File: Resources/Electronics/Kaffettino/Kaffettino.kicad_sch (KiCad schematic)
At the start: 39 parts, among them J2 OSTVN02A150, J3 OSTVN04A150, J4 OSTVN04A150, J5 OSTVN04A150, M1 RFID-RC522, Q1 PN2222A, U1 PCF8574AN, U2 DFR0299, U3 ESP32-38Pin-Wroom, U4 26052

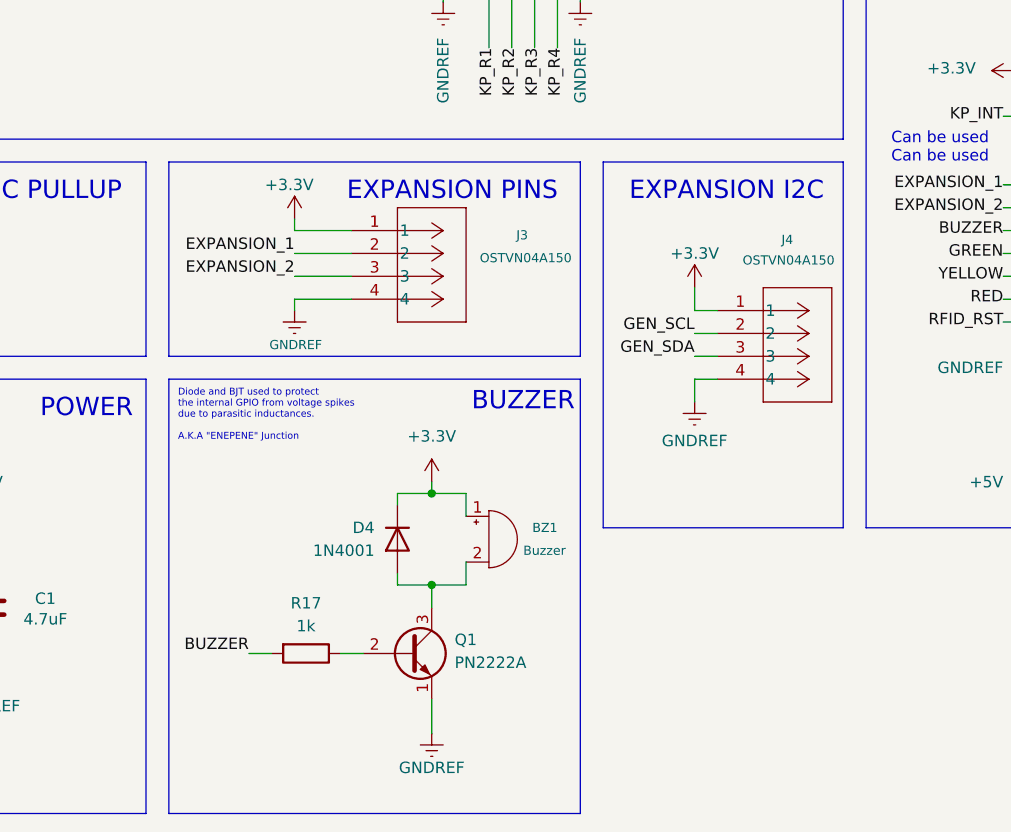
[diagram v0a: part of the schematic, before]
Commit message: Embedded: Added 5V to expansion headers
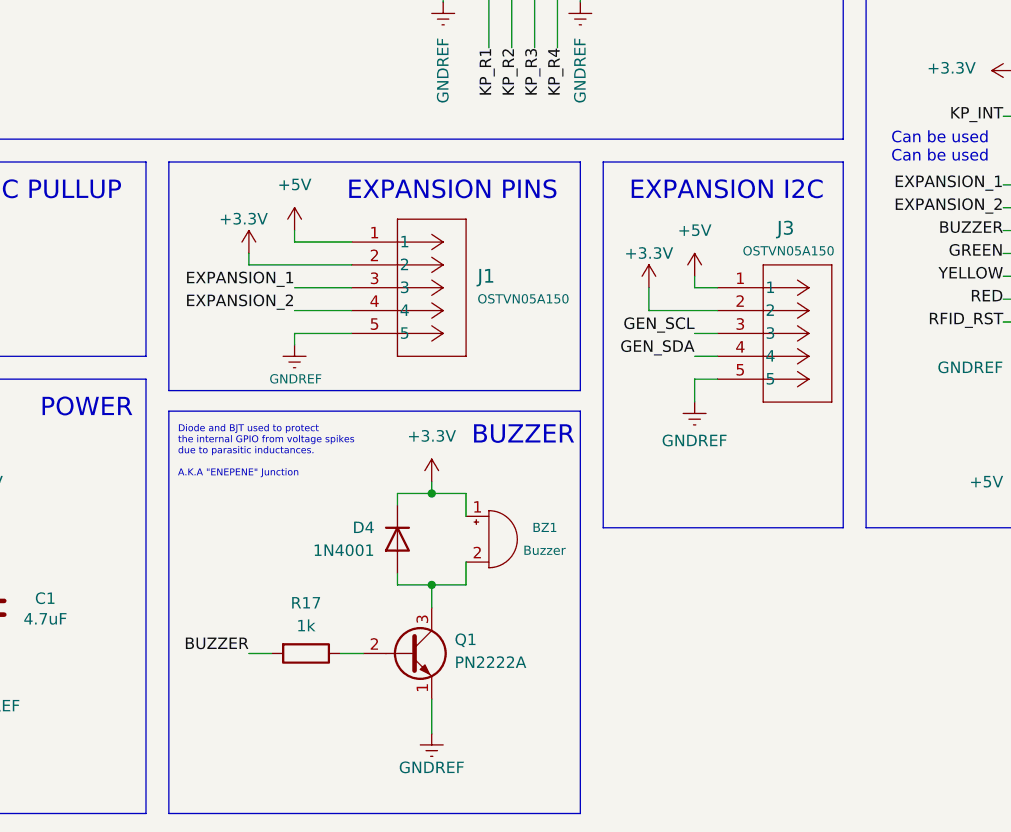
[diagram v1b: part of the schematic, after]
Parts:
- removed J3, J4: OSTVN04A150, OSTVN04A150:CONN_OSTVN04A150_OST, symbol 2025-11-13_14-58-24:OSTVN04A150
- added J1, J3: OSTVN05A150, CONN5_516x256_OST, symbol 2026-02-27_14-49-47:OSTVN05A150
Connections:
- net +3.3V: now also J1.2, J3.2
- net +5V: now also J1.1, J3.1
- net EXPANSION_1: now also J1.3
- net EXPANSION_2: now also J1.4
- net GEN_SCL: now also J3.3
- net GEN_SDA: now also J3.4
- net GNDREF: now also J1.5, J3.5
